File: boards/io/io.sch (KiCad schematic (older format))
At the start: 123 parts, among them J1 61304021021, J2 SSW-120-02-G-D-RA, J4 694106301002, J5 Conn_01x08, J6 SSW-120-02-G-D-RA, J7 Conn_01x08, U1 74LV32APWJ, U10 MC74HC151ADTR2G, U11 SN74LV273APW, U13 IS61C256AL-12TLI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

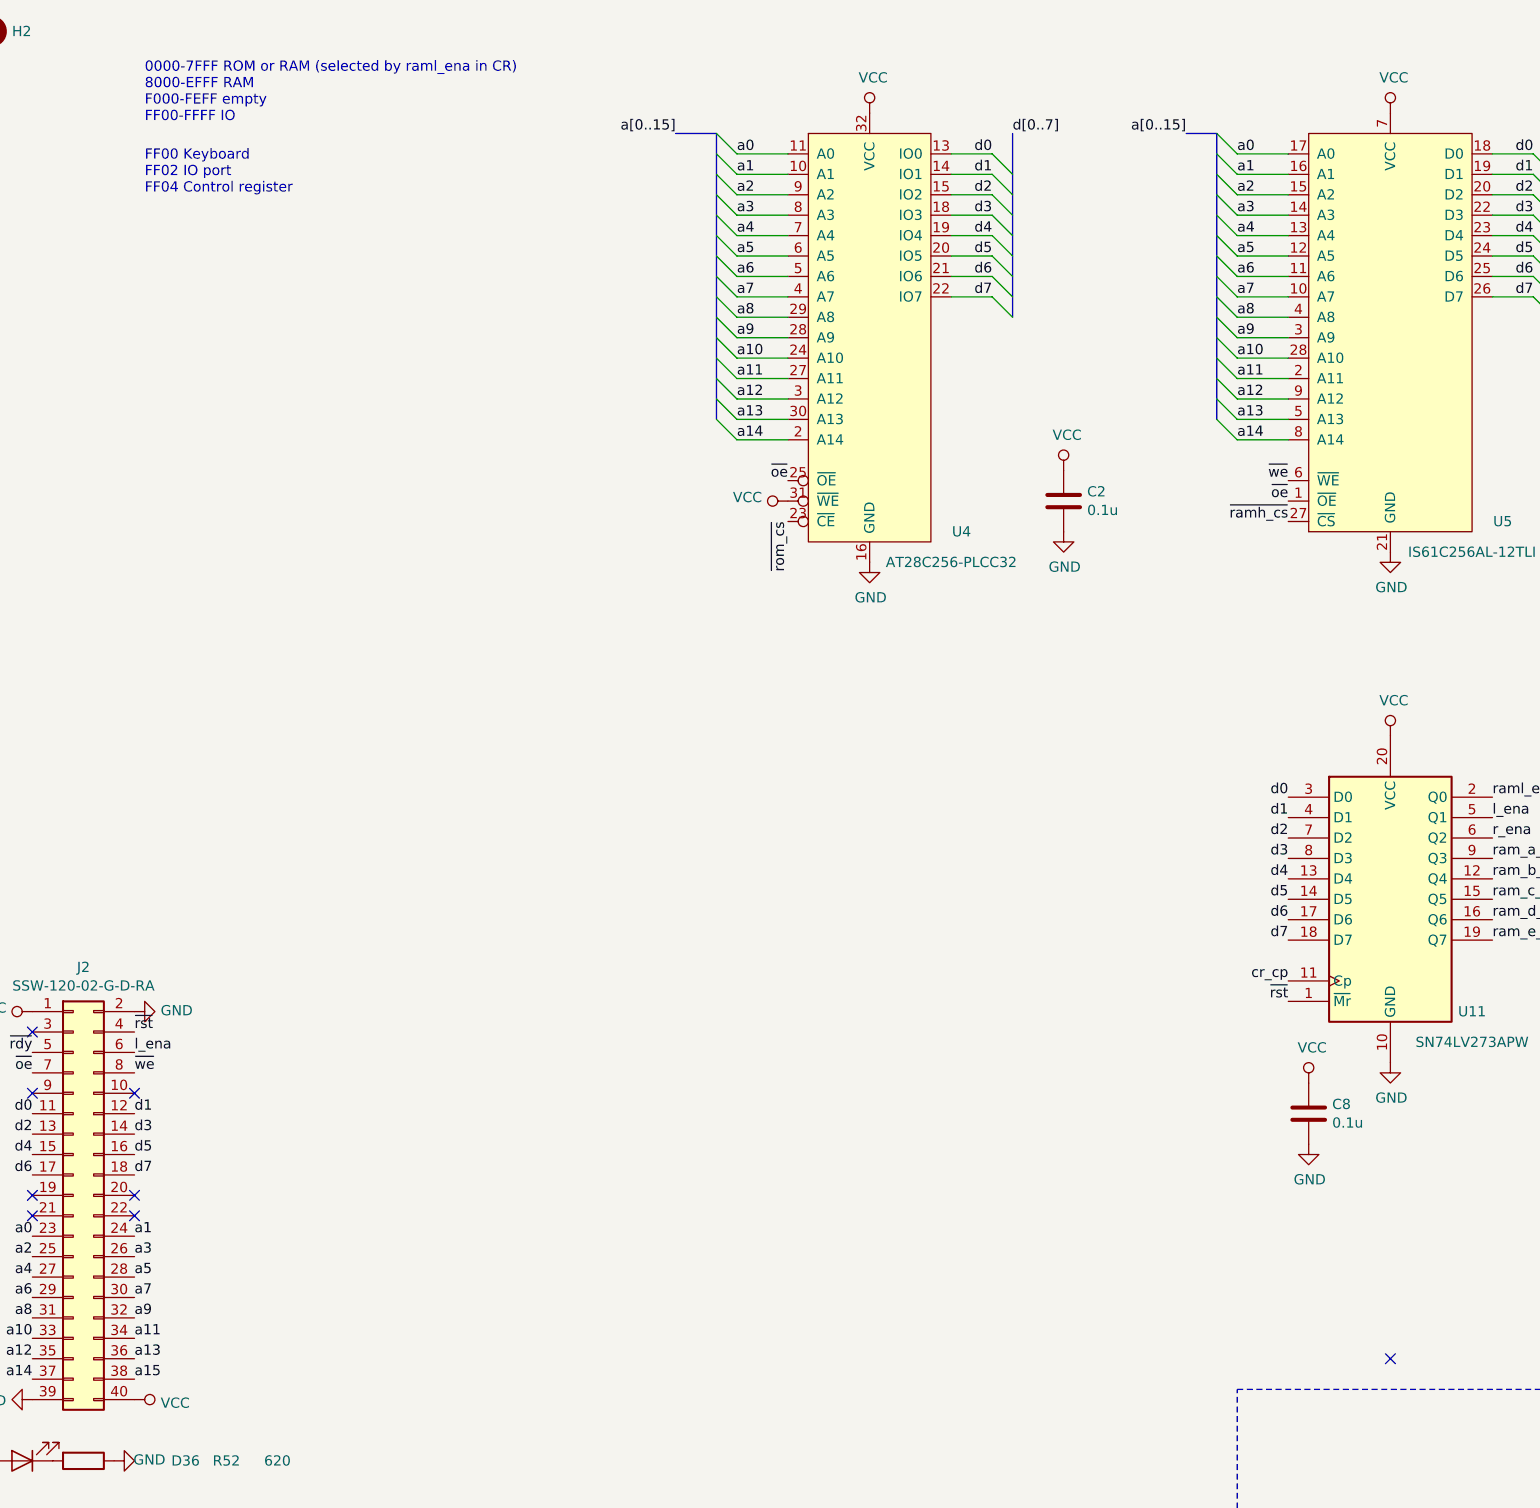
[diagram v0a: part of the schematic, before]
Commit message: IO: fix comment
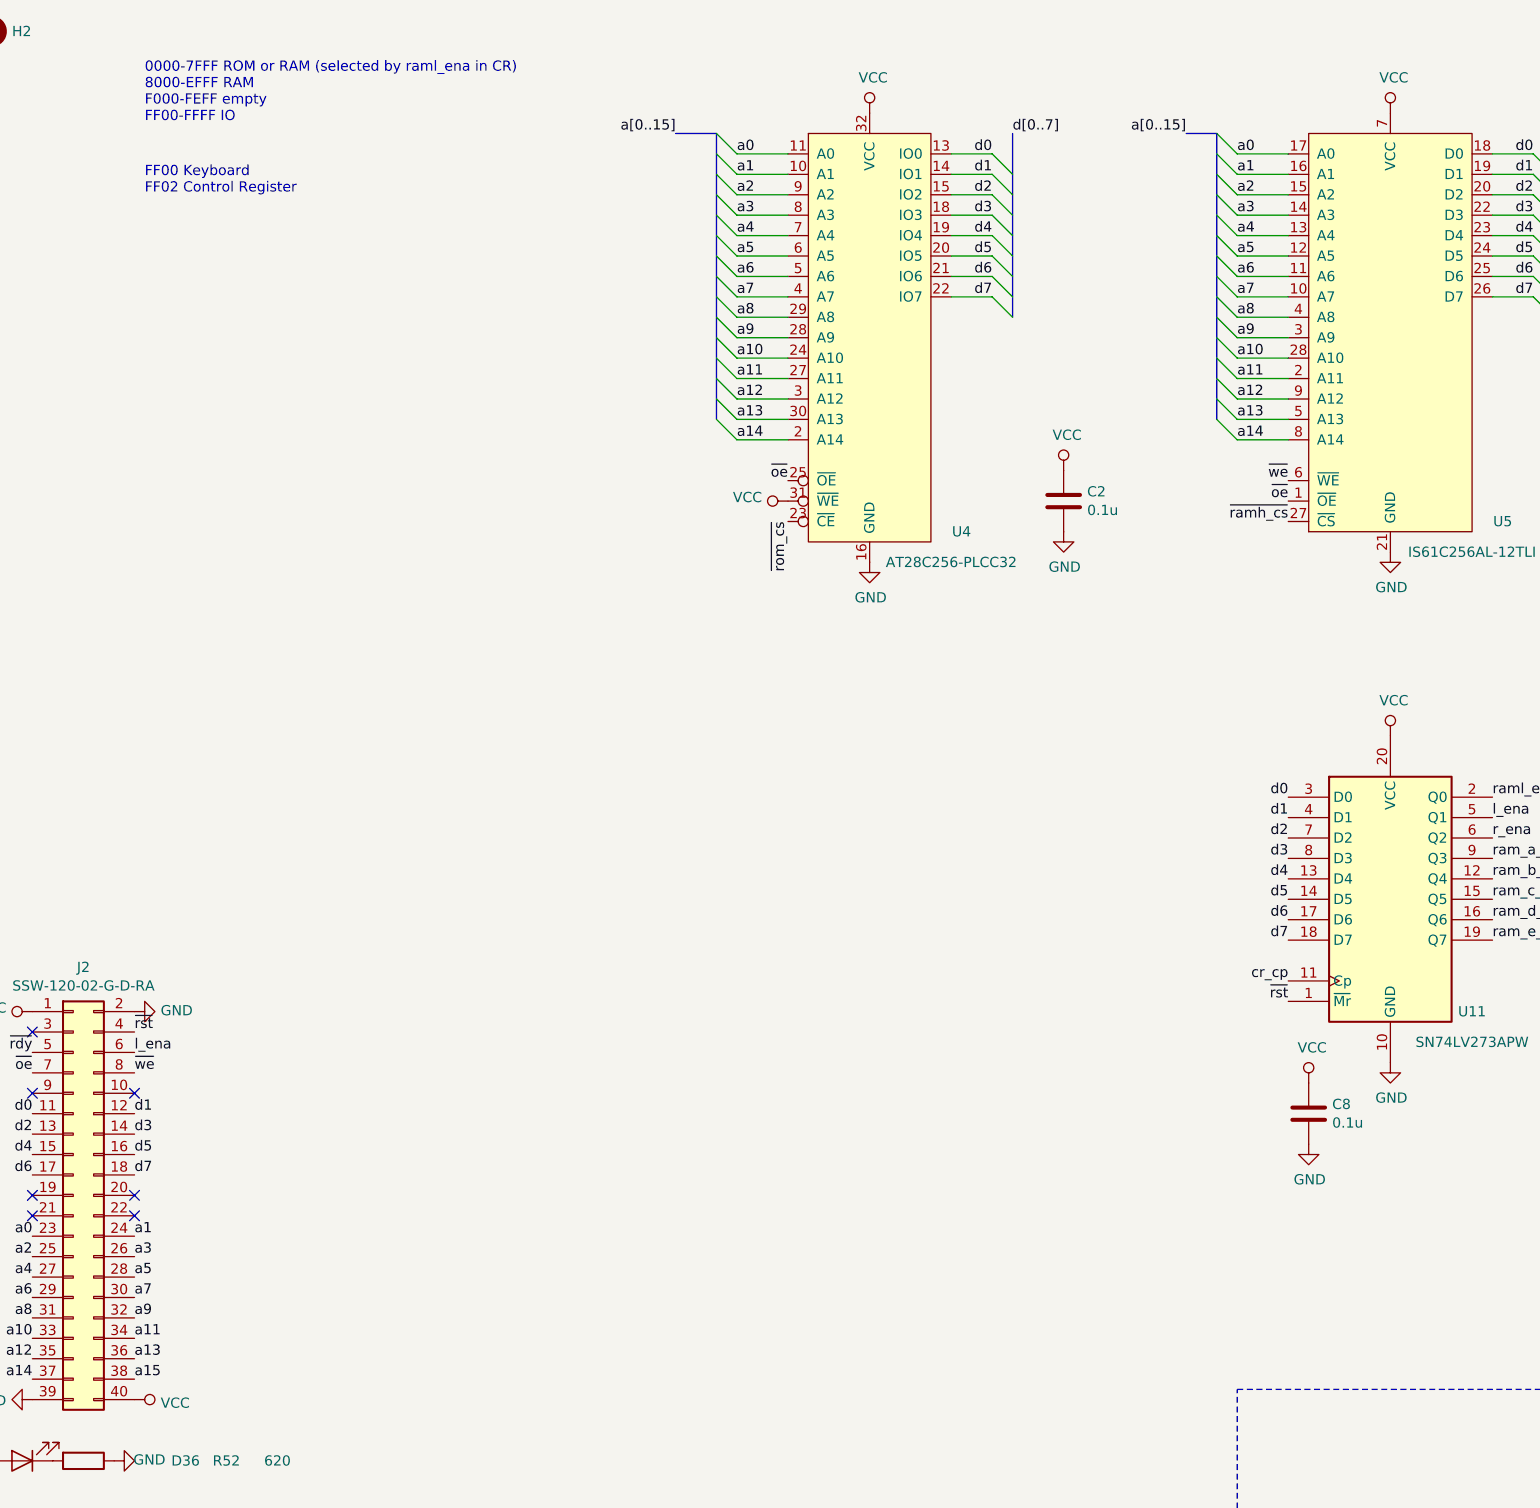
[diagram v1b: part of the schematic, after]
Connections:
- no-connect marks 33 -> 32
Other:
- note added: "FF00 Keyboard\nFF02 Control Register"
- note removed: "FF00 Keyboard\nFF02 IO port\nFF04 Control register"
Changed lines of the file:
@@
 0000-7FFF ROM or RAM (selected by raml_ena in CR)\n8000-EFFF RAM\nF000-FEFF empty\nFF00-FFFF IO\n
 Text Notes 1450 1500 0    50   ~ 0
-FF00 Keyboard\nFF02 IO port\nFF04 Control register
+FF00 Keyboard\nFF02 Control Register
 $Comp
 L 74xx:74LS32 U1
@@
 NoConn ~ 10300 14700
 NoConn ~ 10300 14150
-NoConn ~ 7550 7200
 NoConn ~ 9800 10550
 Wire Wire Line

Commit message: IO board rev. 3
Move side connectors
Take caution against crosstalk
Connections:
- net clk: no longer names the net of J1.3 (Pin_3)
- net ~rdy renamed rdy
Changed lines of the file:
@@
 ~we
 Text Label 12650 1500 3    50   ~ 0
-~rdy
-Text Label 12550 1500 3    50   ~ 0
-clk
+rdy
 Text Label 12550 1000 1    50   ~ 0
 ~rst
@@
 ~we
 Text Label 900  5700 2    50   ~ 0
-~rdy
+rdy
 Text Label 1400 5600 0    50   ~ 0
 ~rst
@@
 ~we
 Text Label 21300 5750 2    50   ~ 0
-~rdy
+rdy
 Text Label 21800 5650 0    50   ~ 0
 ~rst

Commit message: IO: change logic family
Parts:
- U1: value 74LV32APWJ -> 74HC32PW
- U11, U7: value SN74LV273APW -> MC74HC273ADT
- U14: value SN74LV139APW -> SN74HC139PW
- U2: value SN74LV00APW -> 74HC00PW
- U8: value SN74LV244APW -> MC74HC244ADT
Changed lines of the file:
@@
 Sheet 1 1
 Title "IO and memory board"
-Date "2020-12-06"
-Rev "2"
+Date "2021-01-21"
+Rev "3"
 Comp ""
 Comment1 "Licensed under the TAPR Open Hardware License (www.tapr.org/OHL)"
@@
 P 12050 11000
 F 0 "U1" H 12050 11325 50  0000 C CNN
-F 1 "74LV32APWJ" H 12050 11234 50  0000 C CNN
+F 1 "74HC32PW" H 12050 11234 50  0000 C CNN
 F 2 "Package_SO:TSSOP-14_4.4x5mm_P0.65mm" H 12050 11000 50  0001 C CNN
-F 3 "https://www.mouser.de/datasheet/2/916/74LV32A-1597772.pdf" H 12050 11000 50  0001 C CNN
+F 3 "http://www.farnell.com/datasheets/1648978.pdf" H 12050 11000 50  0001 C CNN
 	1    12050 11000
 	1    0    0    -1
@@
 P 8900 8200
 F 0 "U1" H 8900 8525 50  0000 C CNN
-F 1 "74LV32APWJ" H 8900 8434 50  0000 C CNN
+F 1 "74HC32PW" H 8900 8434 50  0000 C CNN
 F 2 "Package_SO:TSSOP-14_4.4x5mm_P0.65mm" H 8900 8200 50  0001 C CNN
-F 3 "https://www.mouser.de/datasheet/2/916/74LV32A-1597772.pdf" H 8900 8200 50  0001 C CNN
+F 3 "http://www.farnell.com/datasheets/1648978.pdf" H 8900 8200 50  0001 C CNN
 	2    8900 8200
 	1    0    0    -1
@@
 P 2650 14100
 F 0 "U1" H 2880 14146 50  0000 L CNN
-F 1 "74LV32APWJ" H 2880 14055 50  0000 L CNN
+F 1 "74HC32PW" H 2880 14055 50  0000 L CNN
 F 2 "Package_SO:TSSOP-14_4.4x5mm_P0.65mm" H 2650 14100 50  0001 C CNN
-F 3 "https://www.mouser.de/datasheet/2/916/74LV32A-1597772.pdf" H 2650 14100 50  0001 C CNN
+F 3 "http://www.farnell.com/datasheets/1648978.pdf" H 2650 14100 50  0001 C CNN
 	5    2650 14100
 	1    0    0    -1
@@
 P 9900 4950
 F 0 "U7" H 10300 4400 50  0000 C CNN
-F 1 "SN74LV273APW" H 10300 4250 50  0000 C CNN
+F 1 "MC74HC273ADT" H 10300 4250 50  0000 C CNN
 F 2 "Package_SO:TSSOP-20_4.4x6.5mm_P0.65mm" H 9900 4950 50  0001 C CNN
-F 3 "https://www.ti.com/lit/ds/symlink/sn74lv273a.pdf" H 9900 4950 50  0001 C CNN
+F 3 "http://www.farnell.com/datasheets/1878567.pdf" H 9900 4950 50  0001 C CNN
 	1    9900 4950
 	1    0    0    -1
@@
 P 13600 4950
 F 0 "U8" H 14000 4400 50  0000 C CNN
-F 1 "SN74LV244APW" H 13950 4250 50  0000 C CNN
+F 1 "MC74HC244ADT" H 13950 4250 50  0000 C CNN
 F 2 "Package_SO:TSSOP-20_4.4x6.5mm_P0.65mm" H 13600 4950 50  0001 C CNN
-F 3 "https://www.ti.com/lit/ds/symlink/sn74lv244a.pdf" H 13600 4950 50  0001 C CNN
+F 3 "http://www.farnell.com/datasheets/1878565.pdf" H 13600 4950 50  0001 C CNN
 	1    13600 4950
 	1    0    0    -1
@@
 P 10800 10450
 F 0 "U1" H 10800 10775 50  0000 C CNN
-F 1 "74LV32APWJ" H 10800 10684 50  0000 C CNN
+F 1 "74HC32PW" H 10800 10684 50  0000 C CNN
 F 2 "Package_SO:TSSOP-14_4.4x5mm_P0.65mm" H 10800 10450 50  0001 C CNN
-F 3 "https://www.mouser.de/datasheet/2/916/74LV32A-1597772.pdf" H 10800 10450 50  0001 C CNN
+F 3 "http://www.farnell.com/datasheets/1648978.pdf" H 10800 10450 50  0001 C CNN
 	3    10800 10450
 	1    0    0    -1
@@
 P 10800 11000
 F 0 "U1" H 10800 11325 50  0000 C CNN
-F 1 "74LV32APWJ" H 10800 11234 50  0000 C CNN
+F 1 "74HC32PW" H 10800 11234 50  0000 C CNN
 F 2 "Package_SO:TSSOP-14_4.4x5mm_P0.65mm" H 10800 11000 50  0001 C CNN
-F 3 "https://www.mouser.de/datasheet/2/916/74LV32A-1597772.pdf" H 10800 11000 50  0001 C CNN
+F 3 "http://www.farnell.com/datasheets/1648978.pdf" H 10800 11000 50  0001 C CNN
 	4    10800 11000
 	1    0    0    -1
@@
 P 7550 4950
 F 0 "U11" H 7950 4400 50  0000 C CNN
-F 1 "SN74LV273APW" H 7950 4250 50  0000 C CNN
+F 1 "MC74HC273ADT" H 7950 4250 50  0000 C CNN
 F 2 "Package_SO:TSSOP-20_4.4x6.5mm_P0.65mm" H 7550 4950 50  0001 C CNN
-F 3 "https://www.ti.com/lit/ds/symlink/sn74lv273a.pdf" H 7550 4950 50  0001 C CNN
+F 3 "http://www.farnell.com/datasheets/1878567.pdf" H 7550 4950 50  0001 C CNN
 	1    7550 4950
 	1    0    0    -1
@@
 P 9300 10450
 F 0 "U14" H 9300 10817 50  0000 C CNN
-F 1 "SN74LV139APW" H 9300 10726 50  0000 C CNN
+F 1 "SN74HC139PW" H 9300 10726 50  0000 C CNN
 F 2 "Package_SO:TSSOP-16_4.4x5mm_P0.65mm" H 9300 10450 50  0001 C CNN
-F 3 "https://www.ti.com/lit/ds/symlink/sn74lv139a.pdf" H 9300 10450 50  0001 C CNN
+F 3 "https://www.ti.com/lit/ds/symlink/sn54hc139-sp.pdf" H 9300 10450 50  0001 C CNN
 	1    9300 10450
 	1    0    0    -1
@@
 P 8700 13250
 F 0 "U14" H 8700 13617 50  0000 C CNN
-F 1 "SN74LV139APW" H 8700 13526 50  0000 C CNN
+F 1 "SN74HC139PW" H 8700 13526 50  0000 C CNN
 F 2 "Package_SO:TSSOP-16_4.4x5mm_P0.65mm" H 8700 13250 50  0001 C CNN
-F 3 "https://www.ti.com/lit/ds/symlink/sn74lv139a.pdf" H 8700 13250 50  0001 C CNN
+F 3 "https://www.ti.com/lit/ds/symlink/sn54hc139-sp.pdf" H 8700 13250 50  0001 C CNN
 	2    8700 13250
 	1    0    0    -1
@@
 P 6750 14100
 F 0 "U14" H 6980 14146 50  0000 L CNN
-F 1 "SN74LV139APW" H 6980 14055 50  0000 L CNN
+F 1 "SN74HC139PW" H 6980 14055 50  0000 L CNN
 F 2 "Package_SO:TSSOP-16_4.4x5mm_P0.65mm" H 6750 14100 50  0001 C CNN
-F 3 "https://www.ti.com/lit/ds/symlink/sn74lv139a.pdf" H 6750 14100 50  0001 C CNN
+F 3 "https://www.ti.com/lit/ds/symlink/sn54hc139-sp.pdf" H 6750 14100 50  0001 C CNN
 	3    6750 14100
 	1    0    0    -1
@@
 P 7950 8700
 F 0 "U2" H 7950 9025 50  0000 C CNN
-F 1 "SN74LV00APW" H 7950 8934 50  0000 C CNN
+F 1 "74HC00PW" H 7950 8934 50  0000 C CNN
 F 2 "Package_SO:TSSOP-14_4.4x5mm_P0.65mm" H 7950 8700 50  0001 C CNN
-F 3 "https://www.ti.com/lit/ds/symlink/sn74lv00a.pdf" H 7950 8700 50  0001 C CNN
+F 3 "http://www.farnell.com/datasheets/1649009.pdf" H 7950 8700 50  0001 C CNN
 	1    7950 8700
 	1    0    0    -1
@@
 P 8900 8800
 F 0 "U2" H 8900 9125 50  0000 C CNN
-F 1 "SN74LV00APW" H 8900 9034 50  0000 C CNN
+F 1 "74HC00PW" H 8900 9034 50  0000 C CNN
 F 2 "Package_SO:TSSOP-14_4.4x5mm_P0.65mm" H 8900 8800 50  0001 C CNN
-F 3 "https://www.ti.com/lit/ds/symlink/sn74lv00a.pdf" H 8900 8800 50  0001 C CNN
+F 3 "http://www.farnell.com/datasheets/1649009.pdf" H 8900 8800 50  0001 C CNN
 	2    8900 8800
 	1    0    0    -1
@@
 P 10000 14700
 F 0 "U2" H 10000 15025 50  0000 C CNN
-F 1 "SN74LV00APW" H 10000 14934 50  0000 C CNN
+F 1 "74HC00PW" H 10000 14934 50  0000 C CNN
 F 2 "Package_SO:TSSOP-14_4.4x5mm_P0.65mm" H 10000 14700 50  0001 C CNN
-F 3 "https://www.ti.com/lit/ds/symlink/sn74lv00a.pdf" H 10000 14700 50  0001 C CNN
+F 3 "http://www.farnell.com/datasheets/1649009.pdf" H 10000 14700 50  0001 C CNN
 	3    10000 14700
 	1    0    0    -1
@@
 P 10000 14150
 F 0 "U2" H 10000 14475 50  0000 C CNN
-F 1 "SN74LV00APW" H 10000 14384 50  0000 C CNN
+F 1 "74HC00PW" H 10000 14384 50  0000 C CNN
 F 2 "Package_SO:TSSOP-14_4.4x5mm_P0.65mm" H 10000 14150 50  0001 C CNN
-F 3 "https://www.ti.com/lit/ds/symlink/sn74lv00a.pdf" H 10000 14150 50  0001 C CNN
+F 3 "http://www.farnell.com/datasheets/1649009.pdf" H 10000 14150 50  0001 C CNN
 	4    10000 14150
 	1    0    0    -1
@@
 P 5600 14100
 F 0 "U2" H 5830 14146 50  0000 L CNN
-F 1 "SN74LV00APW" H 5830 14055 50  0000 L CNN
+F 1 "74HC00PW" H 5830 14055 50  0000 L CNN
 F 2 "Package_SO:TSSOP-14_4.4x5mm_P0.65mm" H 5600 14100 50  0001 C CNN
-F 3 "https://www.ti.com/lit/ds/symlink/sn74lv00a.pdf" H 5600 14100 50  0001 C CNN
+F 3 "http://www.farnell.com/datasheets/1649009.pdf" H 5600 14100 50  0001 C CNN
 	5    5600 14100
 	1    0    0    -1
